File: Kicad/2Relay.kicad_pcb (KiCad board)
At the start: 2 copper layers, 48.3 x 41.9 mm, 24 parts, among them J1 Conn_01x04_Male, J2 Conn_01x02_Male, J3 Conn_01x02_Male, K1 G5Q-1A, K2 G5Q-1A, Q1 MMBT3904, Q2 MMBT3904, U1 ATtiny85V-10S, U2 MAX485E, U3 LTV-827S

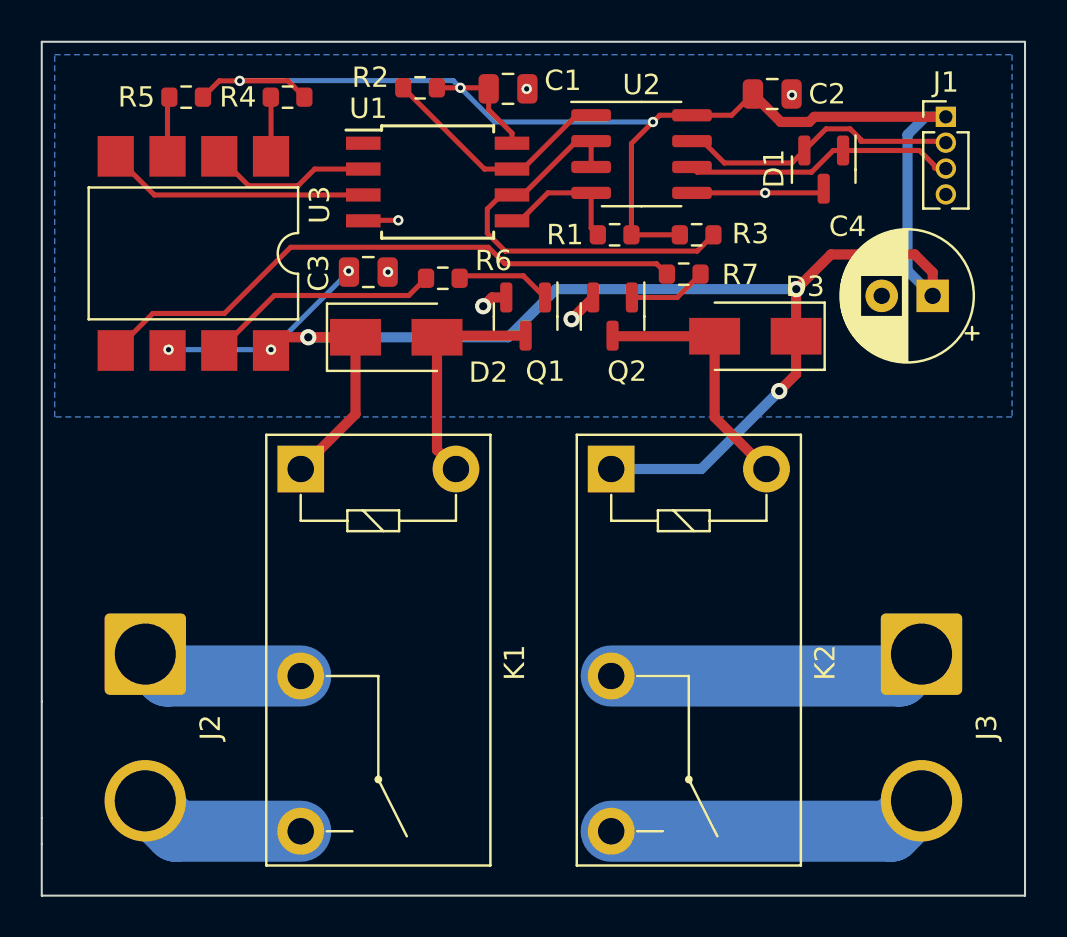
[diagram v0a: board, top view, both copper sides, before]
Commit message: Updated PCB to v0.1.2
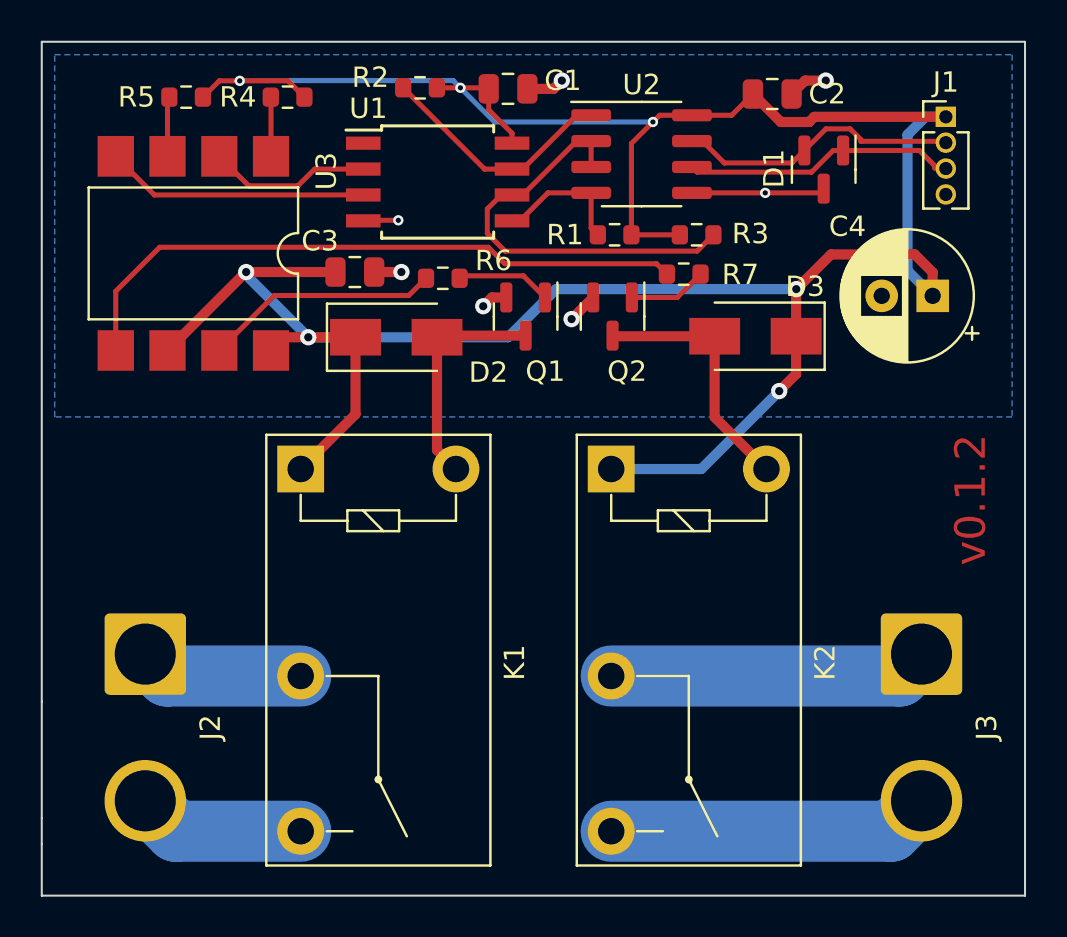
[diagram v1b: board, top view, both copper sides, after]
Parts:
- moved C3 0.66 mm to (97.3, 57.7)
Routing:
- net GND: track 11.1 -> 16.2 mm
- net VCC: track 139.3 -> 143.1 mm, vias 9 -> 7
- net Net-(U3-Pad5): track 29.7 -> 31.4 mm
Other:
- board text added: "v0.1.2"
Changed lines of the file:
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@@
   )
   (footprint "Capacitor_SMD:C_0805_2012Metric" (layer "F.Cu")
-    (at 97.9424 57.658)
+    (at 97.282 57.658)
     (descr "Capacitor SMD 0805 (2012 Metric), square (rectangular) end terminal, IPC_7351 nominal, (Body size source: IPC-SM-782 page 76, https://www.pcb-3d.com/wordpress/wp-content/uploads/ipc-sm-782a_amendment_1_and_2.pdf, https://docs.google.com/spreadsheets/d/1BsfQQcO9C6DZCsRaXUlFlo91Tg2WpOkGARC1WS5S8t0/edit?usp=sharing), generated with kicad-footprint-generator")
     (tags "capacitor")
@@
     (property "Sheetname" "")
     (attr smd)
-    (fp_text reference "C3" (at -2.4384 0.0508 90) (layer "F.SilkS")
+    (fp_text reference "C3" (at -1.712 -1.524 180) (layer "F.SilkS")
       (effects (font (size 1 1) (thickness 0.15)))
     )
@@
     (property "Sheetname" "")
     (attr smd)
-    (fp_text reference "U3" (at -2.3876 -6.1976 90) (layer "F.SilkS")
+    (fp_text reference "U3" (at -4.0386 -6.5278 90) (layer "F.SilkS")
       (effects (font (size 1 1) (thickness 0.15)))
     )
@@
   (gr_line (start 81.915 84.455) (end 81.915 85.725) (layer "Edge.Cuts") (width 0.1))
   (gr_line (start 81.915 84.455) (end 81.915 78.74) (layer "Edge.Cuts") (width 0.1))
+  (gr_text "v0.1.2" (at 127.508 68.834 90) (layer "F.Cu")
+    (effects (font (size 1.5 1.5) (thickness 0.3)))
+  )
   (segment (start 119.5832 50.292) (end 118.1912 50.292) (width 0.5) (layer "F.Cu") (net 1))
   (segment (start 125.64238 58.8264) (end 125.64238 57.67198) (width 0.5) (layer "F.Cu") (net 1))
@@
   (segment (start 115.7782 49.9618) (end 116.8196 48.9204) (width 0.25) (layer "F.Cu") (net 1))
   (segment (start 126.2888 50.038) (end 119.8372 50.038) (width 0.5) (layer "F.Cu") (net 1))
+  (segment (start 96.332 57.658) (end 91.948 57.658) (width 0.5) (layer "F.Cu") (net 1))
   (segment (start 120.65 56.7944) (end 118.9482 58.4962) (width 0.5) (layer "F.Cu") (net 1))
   (segment (start 118.1912 50.292) (end 116.8196 48.9204) (width 0.5) (layer "F.Cu") (net 1))
@@
   (segment (start 112.2426 49.9618) (end 111.9124 50.292) (width 0.25) (layer "F.Cu") (net 1))
   (segment (start 103.8504 49.6976) (end 104.996 50.8432) (width 0.25) (layer "F.Cu") (net 1))
+  (segment (start 91.9378 57.658) (end 88.0872 61.5086) (width 0.5) (layer "F.Cu") (net 1))
+  (segment (start 91.948 57.658) (end 91.9378 57.658) (width 0.5) (layer "F.Cu") (net 1))
   (segment (start 94.00548 48.27328) (end 94.805 49.0728) (width 0.25) (layer "F.Cu") (net 1))
   (segment (start 103.7996 48.6156) (end 103.8504 48.6664) (width 0.25) (layer "F.Cu") (net 1))
   (segment (start 118.9482 58.4962) (end 118.9228 58.5216) (width 0.5) (layer "F.Cu") (net 1))
   (segment (start 102.4636 48.6156) (end 103.7996 48.6156) (width 0.25) (layer "F.Cu") (net 1))
-  (via (at 88.138 61.468) (size 0.508) (drill 0.254) (layers "F.Cu" "B.Cu") (net 1))
   (via (at 91.62992 48.27328) (size 0.508) (drill 0.254) (layers "F.Cu" "B.Cu") (net 1))
-  (via (at 96.9772 57.6072) (size 0.508) (drill 0.254) (layers "F.Cu" "B.Cu") (net 1))
   (via (at 111.9124 50.292) (size 0.508) (drill 0.254) (layers "F.Cu" "B.Cu") (free) (net 1))
   (via (at 118.9482 58.4962) (size 0.8) (drill 0.4) (layers "F.Cu" "B.Cu") (net 1))
+  (via (at 91.948 57.658) (size 0.8) (drill 0.4) (layers "F.Cu" "B.Cu") (net 1))
   (via (at 118.11 63.5) (size 0.8) (drill 0.4) (layers "F.Cu" "B.Cu") (net 1))
   (via (at 94.996 60.8584) (size 0.8) (drill 0.4) (layers "F.Cu" "B.Cu") (net 1))
   (via (at 102.4636 48.6156) (size 0.508) (drill 0.254) (layers "F.Cu" "B.Cu") (net 1))
-  (via (at 93.1672 61.468) (size 0.508) (drill 0.254) (layers "F.Cu" "B.Cu") (net 1))
   (segment (start 125.2888 50.038) (end 126.2888 50.038) (width 0.5) (layer "B.Cu") (net 1))
   (segment (start 104.8004 60.8584) (end 107.1626 58.4962) (width 0.5) (layer "B.Cu") (net 1))
   (segment (start 114.285 67.325) (end 109.865 67.325) (width 0.5) (layer "B.Cu") (net 1))
-  (segment (start 96.9772 57.658) (end 93.1672 61.468) (width 0.25) (layer "B.Cu") (net 1))
   (segment (start 111.9124 50.292) (end 104.14 50.292) (width 0.25) (layer "B.Cu") (net 1))
-  (segment (start 96.9772 57.6072) (end 96.9772 57.658) (width 0.25) (layer "B.Cu") (net 1))
   (segment (start 125.64238 58.8264) (end 124.4092 57.59322) (width 0.5) (layer "B.Cu") (net 1))
   (segment (start 118.11 63.5) (end 114.285 67.325) (width 0.5) (layer "B.Cu") (net 1))
@@
   (segment (start 102.108 48.26) (end 102.4636 48.6156) (width 0.25) (layer "B.Cu") (net 1))
   (segment (start 124.4092 57.59322) (end 124.4092 50.9176) (width 0.5) (layer "B.Cu") (net 1))
+  (segment (start 91.948 57.658) (end 91.948 57.8104) (width 0.5) (layer "B.Cu") (net 1))
   (segment (start 124.4092 50.9176) (end 125.2888 50.038) (width 0.5) (layer "B.Cu") (net 1))
   (segment (start 91.62992 48.27328) (end 91.6432 48.26) (width 0.25) (layer "B.Cu") (net 1))
-  (segment (start 93.1672 61.468) (end 88.138 61.468) (width 0.25) (layer "B.Cu") (net 1))
   (segment (start 91.6432 48.26) (end 102.108 48.26) (width 0.25) (layer "B.Cu") (net 1))
+  (segment (start 91.948 57.8104) (end 94.996 60.8584) (width 0.5) (layer "B.Cu") (net 1))
+  (segment (start 105.7504 48.6664) (end 107.0356 48.6664) (width 0.5) (layer "F.Cu") (net 2))
   (segment (start 104.0107 58.9049) (end 103.5812 59.3344) (width 0.5) (layer "F.Cu") (net 2))
   (segment (start 99.4156 55.118) (end 97.7214 55.118) (width 0.25) (layer "F.Cu") (net 2))
@@
   (segment (start 97.7214 55.118) (end 97.696 55.1434) (width 0.25) (layer "F.Cu") (net 2))
   (segment (start 107.91918 59.96692) (end 108.9812 58.9049) (width 0.5) (layer "F.Cu") (net 2))
+  (segment (start 98.232 57.658) (end 99.568 57.658) (width 0.5) (layer "F.Cu") (net 2))
   (segment (start 120.0889 53.7718) (end 120.2944 53.5663) (width 0.25) (layer "F.Cu") (net 2))
+  (segment (start 119.38 48.26) (end 118.7196 48.9204) (width 0.5) (layer "F.Cu") (net 2))
+  (segment (start 120.396 48.26) (end 119.38 48.26) (width 0.5) (layer "F.Cu") (net 2))
+  (segment (start 107.0356 48.6664) (end 107.442 48.26) (width 0.5) (layer "F.Cu") (net 2))
+  (via (at 120.396 48.26) (size 0.8) (drill 0.4) (layers "F.Cu" "B.Cu") (free) (net 2))
   (via (at 107.91918 59.96692) (size 0.8) (drill 0.4) (layers "F.Cu" "B.Cu") (net 2))
   (via (at 99.4156 55.118) (size 0.508) (drill 0.254) (layers "F.Cu" "B.Cu") (free) (net 2))
-  (via (at 105.7148 48.6664) (size 0.508) (drill 0.254) (layers "F.Cu" "B.Cu") (net 2))
+  (via (at 107.442 48.26) (size 0.8) (drill 0.4) (layers "F.Cu" "B.Cu") (free) (net 2))
   (via (at 103.5812 59.3344) (size 0.8) (drill 0.4) (layers "F.Cu" "B.Cu") (net 2))
-  (via (at 98.9076 57.658) (size 0.508) (drill 0.254) (layers "F.Cu" "B.Cu") (net 2))
+  (via (at 99.568 57.658) (size 0.8) (drill 0.4) (layers "F.Cu" "B.Cu") (free) (net 2))
   (via (at 117.4242 53.7718) (size 0.508) (drill 0.254) (layers "F.Cu" "B.Cu") (net 2))
-  (via (at 118.7348 48.9712) (size 0.508) (drill 0.254) (layers "F.Cu" "B.Cu") (net 2))
   (segment (start 125.73 52.4256) (end 125.73 52.5272) (width 0.25) (layer "F.Cu") (net 3))
   (segment (start 119.698808 52.75332) (end 120.760828 51.6913) (width 0.25) (layer "F.Cu") (net 3))
@@
   (segment (start 99.92868 58.80912) (end 100.775 57.9628) (width 0.25) (layer "F.Cu") (net 13))
   (segment (start 104.64446 57.2516) (end 103.83343 56.44057) (width 0.25) (layer "F.Cu") (net 14))
-  (segment (start 87.3658 59.69) (end 85.5472 61.5086) (width 0.25) (layer "F.Cu") (net 14))
+  (segment (start 112.0912 57.2516) (end 104.64446 57.2516) (width 0.25) (layer "F.Cu") (net 14))
+  (segment (start 87.70443 56.44057) (end 85.5472 58.5978) (width 0.25) (layer "F.Cu") (net 14))
   (segment (start 112.5992 57.7596) (end 112.0912 57.2516) (width 0.25) (layer "F.Cu") (net 14))
-  (segment (start 103.83343 56.44057) (end 94.13063 56.44057) (width 0.25) (layer "F.Cu") (net 14))
-  (segment (start 90.8812 59.69) (end 87.3658 59.69) (width 0.25) (layer "F.Cu") (net 14))
-  (segment (start 94.13063 56.44057) (end 90.8812 59.69) (width 0.25) (layer "F.Cu") (net 14))
-  (segment (start 112.0912 57.2516) (end 104.64446 57.2516) (width 0.25) (layer "F.Cu") (net 14))
+  (segment (start 103.83343 56.44057) (end 87.70443 56.44057) (width 0.25) (layer "F.Cu") (net 14))
+  (segment (start 85.5472 58.5978) (end 85.5472 61.5086) (width 0.25) (layer "F.Cu") (net 14))
   (segment (start 105.55198 57.84288) (end 106.614 58.9049) (width 0.25) (layer "F.Cu") (net 15))
   (segment (start 102.425 57.9628) (end 102.54492 57.84288) (width 0.25) (layer "F.Cu") (net 15))
